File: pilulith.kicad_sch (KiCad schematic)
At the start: 94 parts, among them J101 Conn_01x03_Pin, J103 Conn_ARM_JTAG_SWD_10, Q1 SBC847, SW1 KMT221NG, SW2 KMT221NG, SW3 KMT221NG, SW4 KMT221NG, U1 NRF54L15-QFAA-R, U10 LIS2DH, U102 WLA.04, U103 ATECC608B-MAHDA, U104 LF21115TMR, U105 BME280, U106 MP34DT05TR-A, U2 NPM2100-CAAA-R, Y101 32MHz, Y102 32.768K

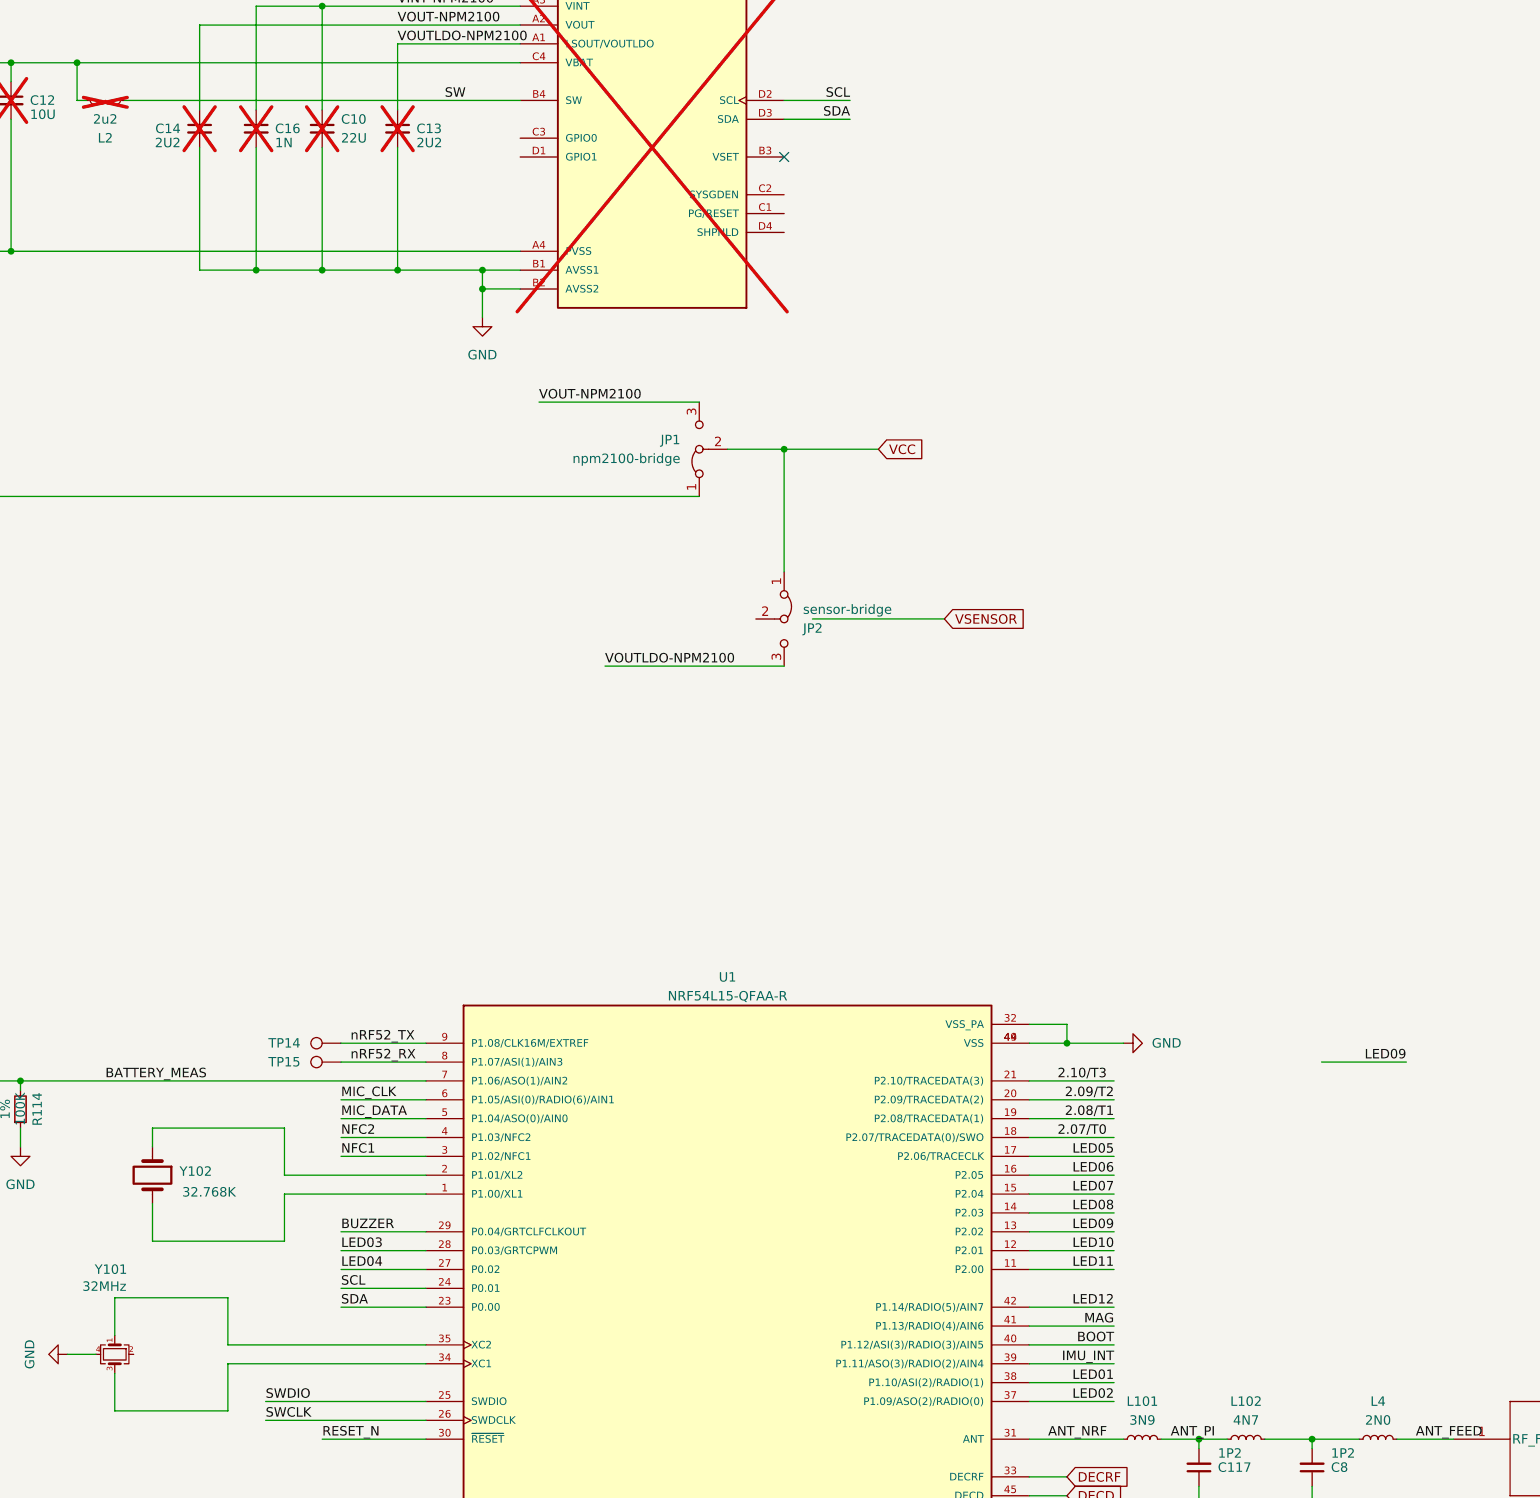
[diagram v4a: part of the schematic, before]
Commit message: fix missing connections on npm2100
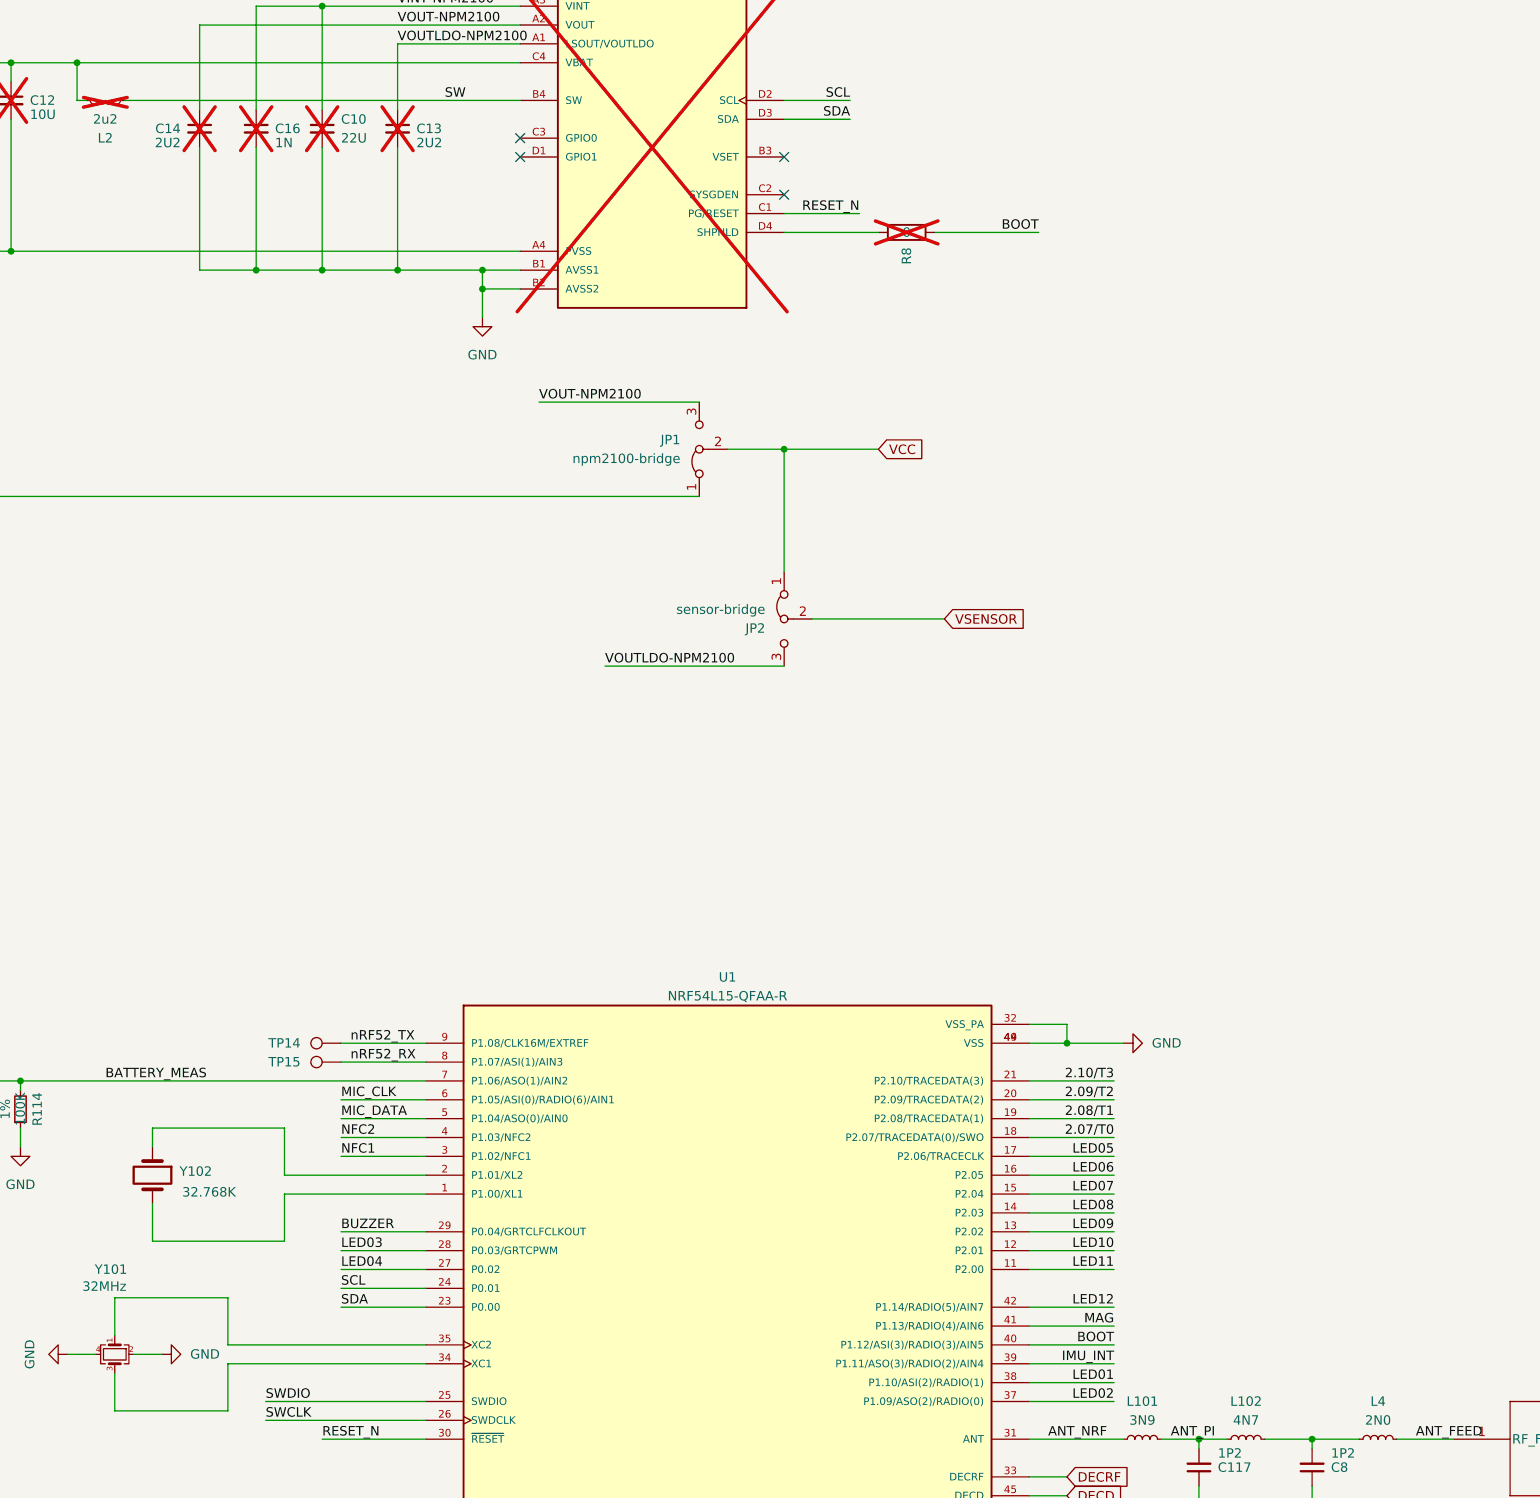
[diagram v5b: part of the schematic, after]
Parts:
- added R8: 0, Resistor_SMD:R_0201_0603Metric, symbol Device:R
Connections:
- net BOOT: now also R8.1
- net GND: now also Y101.2
- net RESET_N: now also U2.C1 (PG/RESET)
- net VSENSOR: now also JP2.2 (C)
- net at U2.D4 (SHPHLD): now also R8.2
- no-connect marks 3 -> 6
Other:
- moved on the sheet: JP2

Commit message: add part info to BOM
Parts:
- C1, C2: Link1 (none) -> https://www.digikey.com/en/products/detail/murata-electroni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; MPN1 (none) -> GRM0335C1H560JA01D; Vendor1 (none) -> Murata
- C10: Link1 (none) -> https://www.digikey.com/en/products/detail/murata-electroni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; MPN1 (none) -> GRM188R61A226ME15D; Vendor1 (none) -> Murata
- C101, C105, C107, C118, C6, C9: Link1 (none) -> https://www.digikey.com/en/products/detail/yageo/CC0201KPX5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; MPN1 (none) -> CC0201KPX5R5BB104; Vendor1 (none) -> YAGEO
- C104: Link1 (none) -> https://www.digikey.com/product-detail/en/GRM155R61A105KE15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; MPN1 (none) -> GRM155R61A105KE15D; Vendor1 (none) -> Murata
- C108, C12: Link1 (none) -> https://www.digikey.com/en/products/detail/murata-electroni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; MPN1 (none) -> GRM155R60J106ME15D; Vendor1 (none) -> Murata
- C11, C16: Link1 (none) -> https://www.digikey.com/en/products/detail/murata-electroni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; MPN1 (none) -> GRM033R71E102KA01D; Vendor1 (none) -> Murata
- C117: value 1P2 -> 0P9; Link1 (none) -> https://www.digikey.com/en/products/detail/murata-electroni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; MPN1 (none) -> GJM0335C1ER90WB01D; Vendor1 (none) -> Murata
- C13, C14: Link1 (none) -> https://www.digikey.com/en/products/detail/murata-electroni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; MPN1 (none) -> GRM155R61A225ME95D; Vendor1 (none) -> Murata
- C29: Link1 (none) -> https://www.digikey.com/product-detail/en/GRM188R6YA475KE15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; MPN1 (none) -> GRM188R6YA475KE15D; Vendor1 (none) -> Murata
- C3, C7: Link1 (none) -> https://www.digikey.com/en/products/detail/murata-electroni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; MPN1 (none) -> GRM033R60J225ME47D; Vendor1 (none) -> Murata
- C4: Link1 (none) -> https://www.digikey.com/en/products/detail/murata-electroni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; MPN1 (none) -> GRM033R71A103KA01D; Vendor1 (none) -> Murata
- C5: Link1 (none) -> https://www.digikey.com/product-detail/en/C0603X7R0J222K030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; MPN1 (none) -> C0603X7R0J222K030BA; Vendor1 (none) -> TDK
- C8: value 1P2 -> 0P6; Link1 (none) -> https://www.digikey.com/product-detail/en/murata-electronic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; MPN1 (none) -> GJM0335C1ER60WB01D; Vendor1 (none) -> Murata
- D101, D102, D103, D104, D105, D106, D107, D108, D109, D110, D111, D112, LED13, LED14, LED15, LED16: value RED -> ORANGE; Link1 (none) -> https://www.digikey.com/en/products/detail/kingbright/APG02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; MPN1 (none) -> APG0201SEC-TT; Vendor1 (none) -> Kingbright
- J101, JP1, JP2: Link1 (none) -> N/A; MPN1 (none) -> N/A; Vendor1 (none) -> N/A
- L1: Link1 (none) -> https://www.digikey.com/en/products/detail/murata-electroni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; MPN1 (none) -> BLM03AG121SN1D; Vendor1 (none) -> Murata
- L101: value 3N9 -> 1N6; Link1 (none) -> https://www.digikey.com/en/products/detail/murata-electroni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; MPN1 (none) -> LQP03TN1N6B02D; Vendor1 (none) -> Murata
- L102: value 4N7 -> 3N3; Link1 (none) -> https://www.digikey.com/en/products/detail/murata-electroni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; MPN1 (none) -> LQP03TN3N3B02D; Vendor1 (none) -> Murata
- L2: Link1 (none) -> https://www.digikey.com/en/products/detail/murata-electroni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; MPN1 (none) -> LQM18PN2R2MFRL; Vendor1 (none) -> Murata
- L3: Link1 (none) -> https://www.digikey.com/en/products/detail/tdk-corporation/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; MPN1 (none) -> MLZ1608M4R7WT000; Vendor1 (none) -> TDK
- L4: value 2N0 -> 1N2; Link1 (none) -> https://www.digikey.com/en/products/detail/murata-electroni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; MPN1 (none) -> LQP03TN1N2B02D; Vendor1 (none) -> Murata
- R1, R101, R102, R103, R104, R105, R106, R107, R108, R109, R110, R111, R112, R2, R3, R5: value R_Small -> 499; Link1 (none) -> https://www.digikey.com/product-detail/en/yageo/RC0201FR-07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; MPN1 (none) -> RC0201FR-07499RL; Vendor1 (none) -> YAGEO
- R113, R114, R115: Link1 (none) -> https://www.digikey.com/en/products/detail/yageo/RC0201FR-0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; MPN1 (none) -> RC0201FR-07100KL; Vendor1 (none) -> YAGEO
- R117, R118: Link1 (none) -> https://www.digikey.com/en/products/detail/yageo/RC0201FR-0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; MPN1 (none) -> RC0201FR-074K7L; Vendor1 (none) -> YAGEO
- R4, R8: Link1 (none) -> https://www.digikey.com/en/products/detail/stackpole-electr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; MPN1 (none) -> RMCF0201ZT0R00; Vendor1 (none) -> Stackpole Electronics Inc
- R7: Link1 https://www.digikey.com/en/products/detail/walsin-technolog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 -> https://www.digikey.com/en/products/detail/yageo/RC0201FR-0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; MPN1 WR04X102 JTL -> RC0201FR-071KL; Vendor1 Walsin Technology Corporation -> YAGEO
- SW1, SW2, SW3: Link1 (none) -> https://www.digikey.com/en/products/detail/c-k/KMT221NG-HF-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; MPN1 (none) -> KMT221NG HF LFS; Vendor1 (none) -> C&K
- SW4: value KMT221NG -> EVP-AWED4A; Link1 (none) -> https://www.digikey.com/en/products/detail/panasonic-electr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; MPN1 (none) -> EVP-AWED4A; Vendor1 (none) -> Panasonic Electronic Components
- U1: Link1 (none) -> https://www.digikey.com/en/products/detail/nordic-semicondu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; MPN1 (none) -> NRF54L15-QFAA-R; Vendor1 (none) -> Nordic Semiconductor ASA
- U102: Link1 (none) -> WLA.04; MPN1 (none) -> WLA.04; Vendor1 (none) -> Taoglas Limited
- U103: Link1 (none) -> https://www.digikey.com/en/products/detail/microchip-techno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; MPN1 (none) -> ATECC608B-MAHDA-T; Vendor1 (none) -> Microchip Technology
- U105: Link1 (none) -> https://www.digikey.com/en/products/detail/bosch-sensortec/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; MPN1 (none) -> BME280; Vendor1 (none) -> Bosch Sensortec
- U106: Link1 (none) -> https://www.digikey.com/en/products/detail/stmicroelectroni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; MPN1 (none) -> MP34DT05TR-A; Vendor1 (none) -> STMicroelectronics
- U2: Link1 (none) -> https://www.digikey.com/en/products/detail/nordic-semicondu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; MPN1 (none) -> NPM2100-CAAA-R; Vendor1 (none) -> Nordic Semiconductor ASA
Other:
- company: (none) -> Golioth
- title: (none) -> Phial
